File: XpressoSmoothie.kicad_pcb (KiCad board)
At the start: 2 copper layers, 99.7 x 99.7 mm, 116 parts, among them J1 HEADER_4, J10 HEADER_3X2, J11 Pwr_in, J12 HEADER_4, J13 HEADER_4, J14 HEADER_3X2, J15 HEADER_4, J16 HEADER_3, J17 HEADER_3, J18 HEADER_3, J19 HEADER_2, J2 HEADER_4, J20 HEADER_2, J21 HEADER_2, J22 HEADER_2, J23 HEADER_3, J24 HEADER_3, J25 HEADER_3, J26 USB, J27 HEADER_4, J3 HEADER_3, J4 HEADER_3X2, J5 HEADER_3X2, J6 LPCXPRESSO_GENERIC_HEADER, J7 HEADER_4, J8 HEADER_4, J9 HEADER_3X2, M1 LOGO_OSHW, M2 LOGO_OSHW, Q1 IRLB 8743, Q2 IRLB 8743, Q3 IRLB 8743, Q4 IRLB 8743, SW1 SW_PUSH, SW2 SW_PUSH, U1 POLOLU_A4988, U10 TC4422A, U11 TC4422A, U12 LM1117-3.3, U2 POLOLU_A4988, U3 POLOLU_A4988, U4 POLOLU_A4988, U5 POLOLU_A4988, U6 CONN_MICROSD, U7 LM7812CT, U8 TC4422A, U9 TC4422A

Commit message: Updated resistor values, calculated based on http://led.linear1.org/1led.wiz. Closes #9.
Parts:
- R18, R19, R21, R23, R28, R29: value 3k3 -> 560
- R30: value 3k3 -> 56
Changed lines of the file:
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@@
-(kicad_pcb (version 3) (host pcbnew "(2013-05-16 BZR 4016)-stable")
+(kicad_pcb (version 3) (host pcbnew "(2013-mar-13)-testing")
   (general
     (links 313)
     (no_connects 11)
-    (area 56.388 53.267 179.864657 163.2712)
+    (area 71.564499 53.784499 171.640501 153.860501)
     (thickness 1.6)
     (drawings 31)
@@
   )
   (setup
-    (last_trace_width 0.889)
+    (last_trace_width 0.635)
     (user_trace_width 0.35)
     (user_trace_width 0.889)
@@
       (effects (font (size 0.50038 0.50038) (thickness 0.10922)))
     )
-    (fp_text value 3k3 (at 0 0.381 90) (layer F.SilkS)
+    (fp_text value 560 (at 0 0.381 90) (layer F.SilkS)
       (effects (font (size 0.50038 0.50038) (thickness 0.10922)))
     )
@@
       (effects (font (size 0.50038 0.50038) (thickness 0.10922)))
     )
-    (fp_text value 3k3 (at 0 0.381 90) (layer F.SilkS)
+    (fp_text value 560 (at 0 0.381 90) (layer F.SilkS)
       (effects (font (size 0.50038 0.50038) (thickness 0.10922)))
     )
@@
       (effects (font (size 0.50038 0.50038) (thickness 0.10922)))
     )
-    (fp_text value 3k3 (at 0 0.381 90) (layer F.SilkS)
+    (fp_text value 560 (at 0 0.381 90) (layer F.SilkS)
       (effects (font (size 0.50038 0.50038) (thickness 0.10922)))
     )
@@
       (effects (font (size 0.50038 0.50038) (thickness 0.10922)))
     )
-    (fp_text value 3k3 (at 0 0.381 90) (layer F.SilkS)
+    (fp_text value 560 (at 0 0.381 90) (layer F.SilkS)
       (effects (font (size 0.50038 0.50038) (thickness 0.10922)))
     )
@@
     (descr "Pololu/Stepstick driver carrier")
     (fp_text reference U2 (at 0 -10.414 180) (layer F.SilkS) hide
-      (effects (font (size 1.524 1.524) (thickness 0.3048)))
+      (effects (font (thickness 0.3048)))
     )
     (fp_text value POLOLU_A4988 (at 0.762 -2.286 180) (layer F.SilkS) hide
-      (effects (font (size 1.524 1.524) (thickness 0.3048)))
+      (effects (font (thickness 0.3048)))
     )
     (fp_line (start -9.652 3.048) (end -8.89 1.778) (layer F.SilkS) (width 0.381))
@@
     (descr "Pololu/Stepstick driver carrier")
     (fp_text reference U4 (at 0 -10.414 180) (layer F.SilkS) hide
-      (effects (font (size 1.524 1.524) (thickness 0.3048)))
+      (effects (font (thickness 0.3048)))
     )
     (fp_text value POLOLU_A4988 (at 0.762 -2.286 180) (layer F.SilkS) hide
-      (effects (font (size 1.524 1.524) (thickness 0.3048)))
+      (effects (font (thickness 0.3048)))
     )
     (fp_line (start -9.652 3.048) (end -8.89 1.778) (layer F.SilkS) (width 0.381))
@@
     (descr "Pololu/Stepstick driver carrier")
     (fp_text reference U5 (at 0 -10.414 180) (layer F.SilkS) hide
-      (effects (font (size 1.524 1.524) (thickness 0.3048)))
+      (effects (font (thickness 0.3048)))
     )
     (fp_text value POLOLU_A4988 (at 0.762 -2.286 180) (layer F.SilkS) hide
-      (effects (font (size 1.524 1.524) (thickness 0.3048)))
+      (effects (font (thickness 0.3048)))
     )
     (fp_line (start -9.652 3.048) (end -8.89 1.778) (layer F.SilkS) (width 0.381))
@@
     (descr "Pololu/Stepstick driver carrier")
     (fp_text reference U1 (at 0 -10.414 270) (layer F.SilkS) hide
-      (effects (font (size 1.524 1.524) (thickness 0.3048)))
+      (effects (font (thickness 0.3048)))
     )
     (fp_text value POLOLU_A4988 (at 0.762 -2.286 270) (layer F.SilkS) hide
-      (effects (font (size 1.524 1.524) (thickness 0.3048)))
+      (effects (font (thickness 0.3048)))
     )
     (fp_line (start -9.652 3.048) (end -8.89 1.778) (layer F.SilkS) (width 0.381))
@@
     (descr "Pololu/Stepstick driver carrier")
     (fp_text reference U3 (at 0 -10.414 180) (layer F.SilkS) hide
-      (effects (font (size 1.524 1.524) (thickness 0.3048)))
+      (effects (font (thickness 0.3048)))
     )
     (fp_text value POLOLU_A4988 (at 0.762 -2.286 180) (layer F.SilkS) hide
-      (effects (font (size 1.524 1.524) (thickness 0.3048)))
+      (effects (font (thickness 0.3048)))
     )
     (fp_line (start -9.652 3.048) (end -8.89 1.778) (layer F.SilkS) (width 0.381))
@@
     (at 104.267 144.78 90)
     (fp_text reference F2 (at -7.493 0 90) (layer F.SilkS)
-      (effects (font (size 1.524 1.524) (thickness 0.3048)))
+      (effects (font (thickness 0.3048)))
     )
     (fp_text value FUSE (at 0 0 90) (layer F.SilkS)
-      (effects (font (size 1.524 1.524) (thickness 0.3048)))
+      (effects (font (thickness 0.3048)))
     )
     (fp_line (start -8.99922 1.50114) (end -8.99922 -1.50114) (layer F.SilkS) (width 0.254))
@@
     (at 84.074 141.605 90)
     (fp_text reference F1 (at -8.763 0 90) (layer F.SilkS)
-      (effects (font (size 1.524 1.524) (thickness 0.3048)))
+      (effects (font (thickness 0.3048)))
     )
     (fp_text value FUSE (at 0 0 90) (layer F.SilkS)
-      (effects (font (size 1.524 1.524) (thickness 0.3048)))
+      (effects (font (thickness 0.3048)))
     )
     (fp_line (start -11.99896 1.50114) (end 11.99896 1.50114) (layer F.SilkS) (width 0.254))
@@
     (at 167.005 87.63 180)
     (fp_text reference J6 (at 5.334 -39.624 180) (layer F.SilkS) hide
-      (effects (font (size 1.524 1.524) (thickness 0.3048)))
+      (effects (font (thickness 0.3048)))
     )
     (fp_text value LPCXPRESSO_GENERIC_HEADER (at 12.954 -36.576 180) (layer F.SilkS) hide
-      (effects (font (size 1.524 1.524) (thickness 0.3048)))
+      (effects (font (thickness 0.3048)))
     )
     (fp_line (start 71.628 0) (end 71.628 -34.29) (layer F.SilkS) (width 0.381))
@@
     )
     (fp_text value Pwr_in (at 0 5.08 90) (layer F.SilkS)
-      (effects (font (size 1.524 1.524) (thickness 0.3048)))
+      (effects (font (thickness 0.3048)))
     )
     (fp_line (start -10.16 -3.81) (end -10.16 3.81) (layer F.SilkS) (width 0.3048))
@@
     (tags DEV)
     (fp_text reference J22 (at 0 -5.08 180) (layer F.SilkS) hide
-      (effects (font (size 1.524 1.524) (thickness 0.3048)))
+      (effects (font (thickness 0.3048)))
     )
     (fp_text value HEADER_2 (at 0 5.08 180) (layer F.SilkS) hide
-      (effects (font (size 1.524 1.524) (thickness 0.3048)))
+      (effects (font (thickness 0.3048)))
     )
     (fp_line (start 5.08 2.54) (end -5.08 2.54) (layer F.SilkS) (width 0.3048))
@@
     (tags DEV)
     (fp_text reference J19 (at 0 -5.08 180) (layer F.SilkS) hide
-      (effects (font (size 1.524 1.524) (thickness 0.3048)))
+      (effects (font (thickness 0.3048)))
     )
     (fp_text value HEADER_2 (at 0 5.08 180) (layer F.SilkS) hide
-      (effects (font (size 1.524 1.524) (thickness 0.3048)))
+      (effects (font (thickness 0.3048)))
     )
     (fp_line (start 5.08 2.54) (end -5.08 2.54) (layer F.SilkS) (width 0.3048))
@@
     (tags DEV)
     (fp_text reference J20 (at 0 -5.08 180) (layer F.SilkS) hide
-      (effects (font (size 1.524 1.524) (thickness 0.3048)))
+      (effects (font (thickness 0.3048)))
     )
     (fp_text value HEADER_2 (at 0 5.08 180) (layer F.SilkS) hide
-      (effects (font (size 1.524 1.524) (thickness 0.3048)))
+      (effects (font (thickness 0.3048)))
     )
     (fp_line (start 5.08 2.54) (end -5.08 2.54) (layer F.SilkS) (width 0.3048))
@@
     (tags DEV)
     (fp_text reference J21 (at 0 -5.08 180) (layer F.SilkS) hide
-      (effects (font (size 1.524 1.524) (thickness 0.3048)))
+      (effects (font (thickness 0.3048)))
     )
     (fp_text value HEADER_2 (at 0 5.08 180) (layer F.SilkS) hide
-      (effects (font (size 1.524 1.524) (thickness 0.3048)))
+      (effects (font (thickness 0.3048)))
     )
     (fp_line (start 5.08 2.54) (end -5.08 2.54) (layer F.SilkS) (width 0.3048))
@@
       (effects (font (size 0.50038 0.50038) (thickness 0.10922)))
     )
-    (fp_text value 3k3 (at 0 0.381 180) (layer F.SilkS)
+    (fp_text value 560 (at 0 0.381 180) (layer F.SilkS)
       (effects (font (size 0.50038 0.50038) (thickness 0.10922)))
     )
@@
       (effects (font (size 0.50038 0.50038) (thickness 0.10922)))
     )
-    (fp_text value 3k3 (at 0 0.381 90) (layer F.SilkS)
+    (fp_text value 560 (at 0 0.381 90) (layer F.SilkS)
       (effects (font (size 0.50038 0.50038) (thickness 0.10922)))
     )
@@
       (effects (font (size 0.50038 0.50038) (thickness 0.10922)))
     )
-    (fp_text value 3k3 (at 0 0.381 180) (layer F.SilkS)
+    (fp_text value 56 (at 0 0.381 180) (layer F.SilkS)
       (effects (font (size 0.50038 0.50038) (thickness 0.10922)))
     )
@@
     )
     (fp_text user hardware (at -0.64516 8.30072 90) (layer F.SilkS)
-      (effects (font (size 1.524 1.524) (thickness 0.3048)))
+      (effects (font (thickness 0.3048)))
     )
     (fp_text user "open source" (at -0.09906 6.20014 90) (layer F.SilkS)
-      (effects (font (size 1.524 1.524) (thickness 0.3048)))
+      (effects (font (thickness 0.3048)))
     )
     (fp_poly (pts (xy -3.37312 4.99872) (xy -3.3147 4.96824) (xy -3.18516 4.88696) (xy -2.99974 4.76504)
@@
   (segment (start 109.855 92.075) (end 109.855 93.98) (width 0.889) (layer F.Cu) (net 118))
   (segment (start 97.79 80.01) (end 109.855 92.075) (width 0.889) (layer F.Cu) (net 118))
-  (segment (start 104.775 93.98) (end 104.775 91.44) (width 0.889) (layer B.Cu) (net 119) (status 400000))
+  (segment (start 104.775 93.98) (end 104.775 91.44) (width 0.889) (layer B.Cu) (net 119))
   (segment (start 94.615 81.28) (end 94.615 80.01) (width 0.889) (layer B.Cu) (net 119))
   (segment (start 104.775 91.44) (end 94.615 81.28) (width 0.889) (layer B.Cu) (net 119))

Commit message: Switched over to minimal Molex SD card connector.
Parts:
- removed U6: CONN_MICROSD, TRANSFLASH_MICROSD
- added J28: MICROSD-MOLEX, microsd-molex-47309, F.Cu at (155.7, 103.5)
- moved C22 6.37 mm to (146.6, 104.1)
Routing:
- net MISO: track 41.2 -> 18.0 mm
- net SCK: track 35.9 -> 21.5 mm
- net GND: track 822.2 -> 808.0 mm, vias 1 -> 0
- net VIO3V3: track 408.3 -> 395.3 mm
- net SD_card_detect: track 19.9 -> 32.7 mm, vias 1 -> 0
- net MOSI: track 19.0 -> 9.32 mm
- net CS: track 37.1 -> 40.7 mm, vias 0 -> 1

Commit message: Fixed resistor values.
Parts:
- R18, R19, R21, R23, R28, R29: value 560 -> 3k3
- R30: value 56 -> 3k3
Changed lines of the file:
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@@
   )
   (setup
-    (last_trace_width 0.35)
+    (last_trace_width 0.635)
     (user_trace_width 0.35)
     (user_trace_width 0.889)
@@
       (effects (font (size 0.50038 0.50038) (thickness 0.10922)))
     )
-    (fp_text value 560 (at 0 0.381 90) (layer F.SilkS)
+    (fp_text value 3k3 (at 0 0.381 90) (layer F.SilkS)
       (effects (font (size 0.50038 0.50038) (thickness 0.10922)))
     )
@@
       (effects (font (size 0.50038 0.50038) (thickness 0.10922)))
     )
-    (fp_text value 560 (at 0 0.381 90) (layer F.SilkS)
+    (fp_text value 3k3 (at 0 0.381 90) (layer F.SilkS)
       (effects (font (size 0.50038 0.50038) (thickness 0.10922)))
     )
@@
       (effects (font (size 0.50038 0.50038) (thickness 0.10922)))
     )
-    (fp_text value 560 (at 0 0.381 90) (layer F.SilkS)
+    (fp_text value 3k3 (at 0 0.381 90) (layer F.SilkS)
       (effects (font (size 0.50038 0.50038) (thickness 0.10922)))
     )
@@
       (effects (font (size 0.50038 0.50038) (thickness 0.10922)))
     )
-    (fp_text value 560 (at 0 0.381 90) (layer F.SilkS)
+    (fp_text value 3k3 (at 0 0.381 90) (layer F.SilkS)
       (effects (font (size 0.50038 0.50038) (thickness 0.10922)))
     )
@@
       (effects (font (size 0.50038 0.50038) (thickness 0.10922)))
     )
-    (fp_text value 560 (at 0 0.381 180) (layer F.SilkS)
+    (fp_text value 3k3 (at 0 0.381 180) (layer F.SilkS)
       (effects (font (size 0.50038 0.50038) (thickness 0.10922)))
     )
@@
       (effects (font (size 0.50038 0.50038) (thickness 0.10922)))
     )
-    (fp_text value 560 (at 0 0.381 90) (layer F.SilkS)
+    (fp_text value 3k3 (at 0 0.381 90) (layer F.SilkS)
       (effects (font (size 0.50038 0.50038) (thickness 0.10922)))
     )
@@
       (effects (font (size 0.50038 0.50038) (thickness 0.10922)))
     )
-    (fp_text value 56 (at 0 0.381 180) (layer F.SilkS)
+    (fp_text value 3k3 (at 0 0.381 180) (layer F.SilkS)
       (effects (font (size 0.50038 0.50038) (thickness 0.10922)))
     )

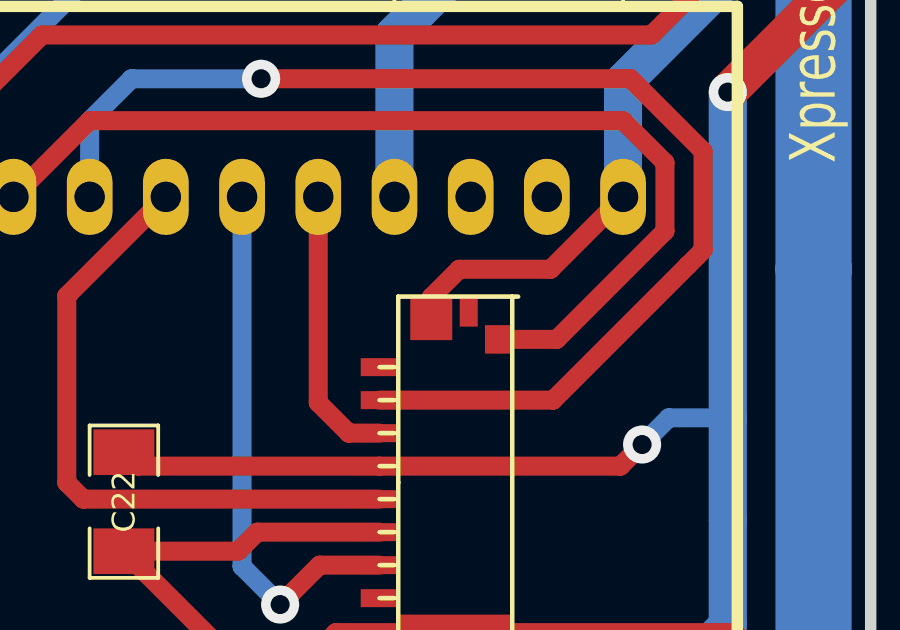
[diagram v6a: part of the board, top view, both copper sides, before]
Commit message: Fixed Molex MicroSD holder. Closes #8.
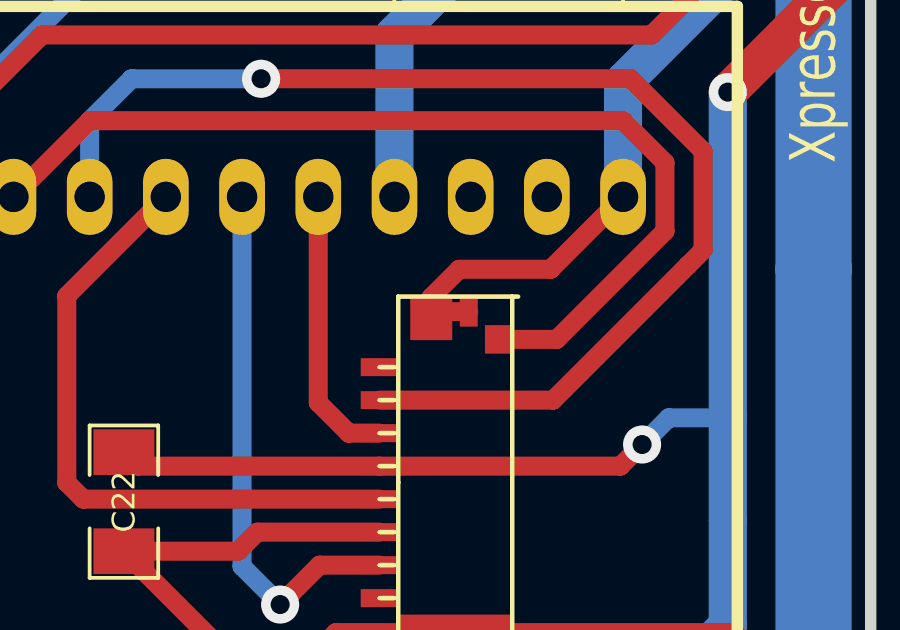
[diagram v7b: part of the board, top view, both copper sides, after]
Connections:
- J28 pad POL: (no net) -> GND
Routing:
- net GND: track 808.0 -> 809.3 mm
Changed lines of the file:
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@@
 (kicad_pcb (version 3) (host pcbnew "(2013-mar-13)-testing")
   (general
-    (links 312)
+    (links 313)
     (no_connects 11)
     (area 71.564499 53.784499 171.640501 153.860501)
     (thickness 1.6)
     (drawings 31)
-    (tracks 1078)
+    (tracks 1080)
     (zones 0)
     (modules 116)
@@
     (pad POL smd rect (at 5.7 2.35) (size 0.6 1)
       (layers F.Cu F.Paste F.Mask)
+      (net 17 GND)
     )
     (pad GND smd rect (at 5.475 1.1 90) (size 1.45 1.4)
@@
   (segment (start 165.354 96.266) (end 165.862 95.758) (width 0.635) (layer F.Cu) (net 16))
   (segment (start 160.865 100.755) (end 165.354 96.266) (width 0.635) (layer F.Cu) (net 16))
+  (segment (start 158.052 97.805) (end 157.027 97.805) (width 0.635) (layer F.Cu) (net 17))
+  (segment (start 157.027 97.805) (end 156.802 98.03) (width 0.635) (layer F.Cu) (net 17))
   (segment (start 156.802 98.03) (end 156.802 97.325) (width 0.635) (layer F.Cu) (net 17))
   (segment (start 160.782 96.393) (end 163.195 93.98) (width 0.635) (layer F.Cu) (net 17))

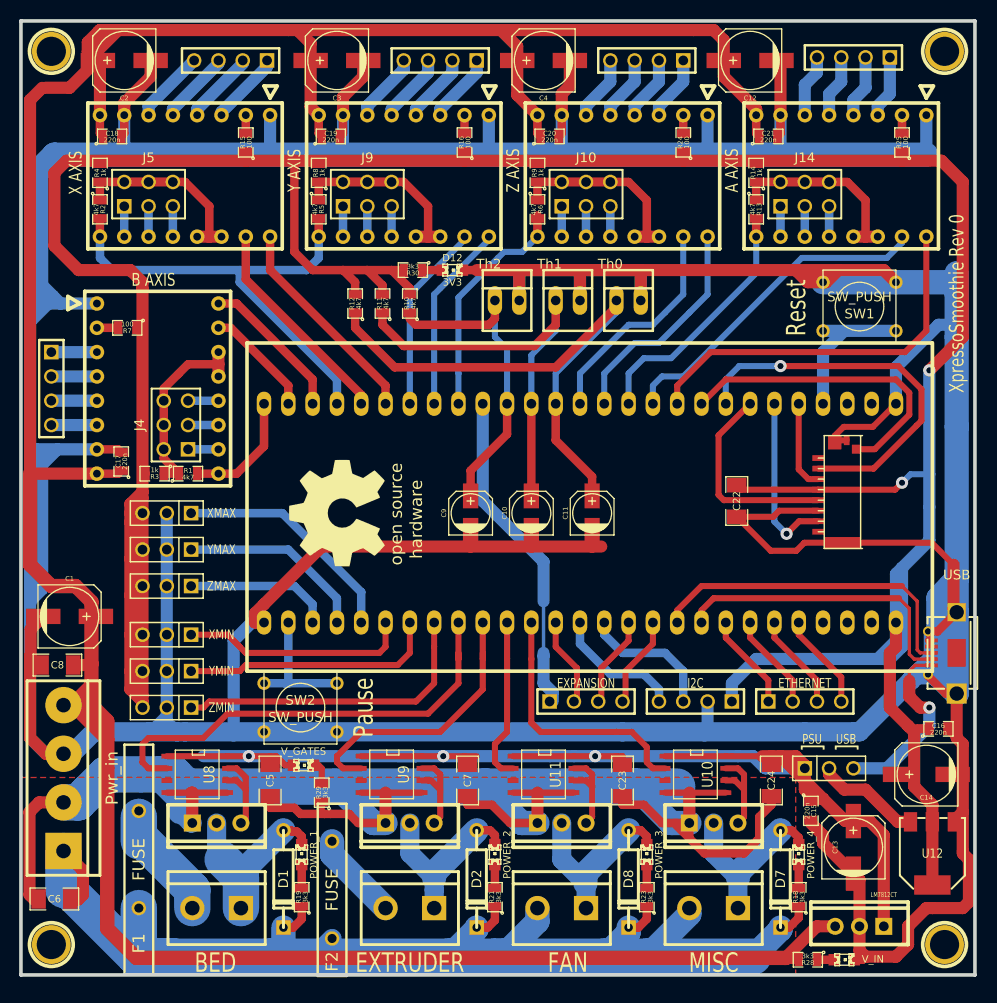
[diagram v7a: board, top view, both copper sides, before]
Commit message: shifted uSD
shifted uSD holder more to the edge, changed resistor values (yet again)
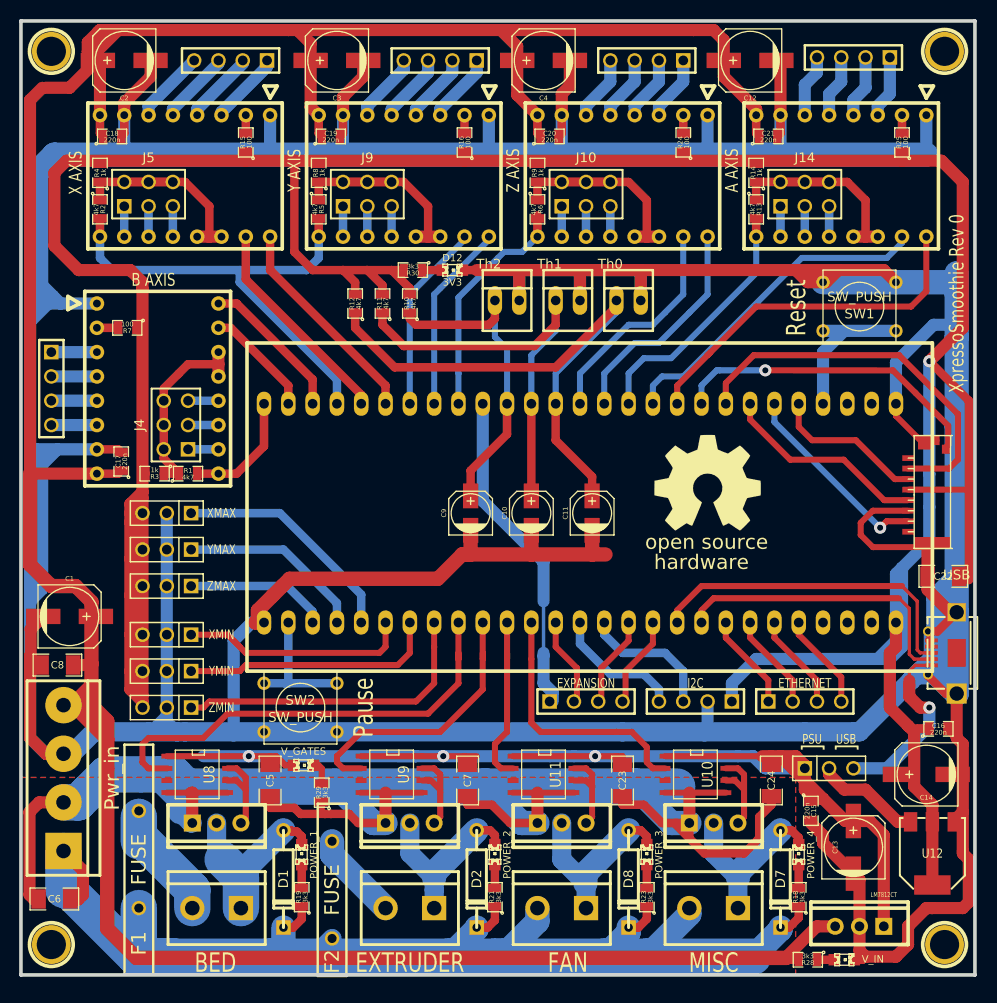
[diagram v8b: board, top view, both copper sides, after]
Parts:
- moved M2 38.9 mm to (143.5, 102.2), turned to 0 degrees
- moved C22 23.0 mm to (168.1, 112.0), turned to 180 degrees
- moved J28 9.40 mm to (165.1, 103.5)
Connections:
- Hole1 pad 1: N-00000131 -> (no net)
- Hole2 pad 1: N-00000130 -> (no net)
- Hole3 pad 1: N-00000129 -> (no net)
- Hole4 pad 1: N-00000128 -> (no net)
- J28 pad 1: N-0000073 -> (no net)
- J28 pad 8: N-0000076 -> (no net)
- J6 pad 2: N-00000127 -> (no net)
- J6 pad 29: N-00000123 -> (no net)
- J6 pad 3: N-00000126 -> (no net)
- J6 pad 30: N-00000125 -> (no net)
- J6 pad 31: N-00000124 -> (no net)
- U10 pad 3: N-0000046 -> (no net)
- U11 pad 3: N-0000045 -> (no net)
- U8 pad 3: N-0000048 -> (no net)
- U9 pad 3: N-0000044 -> (no net)
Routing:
- net GND: track 809.3 -> 794.7 mm
- net VIO3V3: track 395.3 -> 406.5 mm, vias 2 -> 1
- net MOSI: track 9.32 -> 16.1 mm
- net MISO: track 18.0 -> 20.7 mm
- net A-DIR: track 40.1 -> 38.2 mm
- net SD_card_detect: track 32.7 -> 33.3 mm, vias 0 -> 1
- net CS: track 40.7 -> 40.5 mm, vias 1 -> 0
